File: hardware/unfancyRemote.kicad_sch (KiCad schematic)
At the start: 32 parts, among them J1 Arduino Analog, J2 Arduino Digital, J3 HALL1, J4 HALL2, J5 PPM, J6 Conn_01x02, Q1 AO3401A, Q2 MMBT3904, SW1 SW_Push, U1 E28-2G4M12S

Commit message: Fixed R and Cs footprint
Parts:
- C1, C2, C3, C4, C5, C6, C7: footprint Capacitor_SMD:C_0201_0603Metric -> Capacitor_SMD:C_0603_1608Metric
- R1, R10, R2, R3, R5, R6, R7, R8, R9: footprint Resistor_SMD:R_0201_0603Metric -> Resistor_SMD:R_0603_1608Metric
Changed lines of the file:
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@@
       (effects (font (size 1.27 1.27)) (justify left))
     )
-    (property "Footprint" "Capacitor_SMD:C_0201_0603Metric" (id 2) (at 31.4452 95.25 0)
+    (property "Footprint" "Capacitor_SMD:C_0603_1608Metric" (id 2) (at 31.4452 95.25 0)
       (effects (font (size 1.27 1.27)) hide)
     )
@@
     (property "Reference" "R10" (id 0) (at 219.71 151.13 90))
     (property "Value" "220" (id 1) (at 219.71 153.67 90))
-    (property "Footprint" "Resistor_SMD:R_0201_0603Metric" (id 2) (at 219.71 159.258 90)
+    (property "Footprint" "Resistor_SMD:R_0603_1608Metric" (id 2) (at 219.71 159.258 90)
       (effects (font (size 1.27 1.27)) hide)
     )
@@
     (property "Reference" "R8" (id 0) (at 219.71 130.81 90))
     (property "Value" "220" (id 1) (at 219.71 133.35 90))
-    (property "Footprint" "Resistor_SMD:R_0201_0603Metric" (id 2) (at 219.71 138.938 90)
+    (property "Footprint" "Resistor_SMD:R_0603_1608Metric" (id 2) (at 219.71 138.938 90)
       (effects (font (size 1.27 1.27)) hide)
     )
@@
       (effects (font (size 1.27 1.27)) (justify left))
     )
-    (property "Footprint" "Capacitor_SMD:C_0201_0603Metric" (id 2) (at 44.1452 95.25 0)
+    (property "Footprint" "Capacitor_SMD:C_0603_1608Metric" (id 2) (at 44.1452 95.25 0)
       (effects (font (size 1.27 1.27)) hide)
     )
@@
     (property "Reference" "R7" (id 0) (at 219.71 119.38 90))
     (property "Value" "220" (id 1) (at 219.71 121.92 90))
-    (property "Footprint" "Resistor_SMD:R_0201_0603Metric" (id 2) (at 219.71 127.508 90)
+    (property "Footprint" "Resistor_SMD:R_0603_1608Metric" (id 2) (at 219.71 127.508 90)
       (effects (font (size 1.27 1.27)) hide)
     )
@@
     (property "Reference" "R3" (id 0) (at 115.57 149.86 90))
     (property "Value" "10K" (id 1) (at 115.57 152.4 90))
-    (property "Footprint" "Resistor_SMD:R_0201_0603Metric" (id 2) (at 115.57 157.988 90)
+    (property "Footprint" "Resistor_SMD:R_0603_1608Metric" (id 2) (at 115.57 157.988 90)
       (effects (font (size 1.27 1.27)) hide)
     )
@@
       (effects (font (size 1.27 1.27)) (justify left))
     )
-    (property "Footprint" "Capacitor_SMD:C_0201_0603Metric" (id 2) (at 36.5252 156.21 0)
+    (property "Footprint" "Capacitor_SMD:C_0603_1608Metric" (id 2) (at 36.5252 156.21 0)
       (effects (font (size 1.27 1.27)) hide)
     )
@@
       (effects (font (size 1.27 1.27)) (justify left))
     )
-    (property "Footprint" "Resistor_SMD:R_0201_0603Metric" (id 2) (at 132.842 162.56 90)
+    (property "Footprint" "Resistor_SMD:R_0603_1608Metric" (id 2) (at 132.842 162.56 90)
       (effects (font (size 1.27 1.27)) hide)
     )
@@
       (effects (font (size 1.27 1.27)) (justify left))
     )
-    (property "Footprint" "Capacitor_SMD:C_0201_0603Metric" (id 2) (at 37.7952 124.46 0)
+    (property "Footprint" "Capacitor_SMD:C_0603_1608Metric" (id 2) (at 37.7952 124.46 0)
       (effects (font (size 1.27 1.27)) hide)
     )
@@
     (property "Reference" "R6" (id 0) (at 140.97 149.86 90))
     (property "Value" "220" (id 1) (at 140.97 152.4 90))
-    (property "Footprint" "Resistor_SMD:R_0201_0603Metric" (id 2) (at 140.97 157.988 90)
+    (property "Footprint" "Resistor_SMD:R_0603_1608Metric" (id 2) (at 140.97 157.988 90)
       (effects (font (size 1.27 1.27)) hide)
     )
@@
       (effects (font (size 1.27 1.27)) (justify left))
     )
-    (property "Footprint" "Resistor_SMD:R_0201_0603Metric" (id 2) (at 102.362 134.62 90)
+    (property "Footprint" "Resistor_SMD:R_0603_1608Metric" (id 2) (at 102.362 134.62 90)
       (effects (font (size 1.27 1.27)) hide)
     )
@@
       (effects (font (size 1.27 1.27)) (justify left))
     )
-    (property "Footprint" "Capacitor_SMD:C_0201_0603Metric" (id 2) (at 56.8452 95.25 0)
+    (property "Footprint" "Capacitor_SMD:C_0603_1608Metric" (id 2) (at 56.8452 95.25 0)
       (effects (font (size 1.27 1.27)) hide)
     )
@@
       (effects (font (size 1.27 1.27)) (justify left))
     )
-    (property "Footprint" "Capacitor_SMD:C_0201_0603Metric" (id 2) (at 46.6852 124.46 0)
+    (property "Footprint" "Capacitor_SMD:C_0603_1608Metric" (id 2) (at 46.6852 124.46 0)
       (effects (font (size 1.27 1.27)) hide)
     )
@@
       (effects (font (size 1.27 1.27)) (justify left))
     )
-    (property "Footprint" "Resistor_SMD:R_0201_0603Metric" (id 2) (at 89.662 153.67 90)
+    (property "Footprint" "Resistor_SMD:R_0603_1608Metric" (id 2) (at 89.662 153.67 90)
       (effects (font (size 1.27 1.27)) hide)
     )
@@
     (property "Reference" "R9" (id 0) (at 219.71 142.24 90))
     (property "Value" "220" (id 1) (at 219.71 144.78 90))
-    (property "Footprint" "Resistor_SMD:R_0201_0603Metric" (id 2) (at 219.71 150.368 90)
+    (property "Footprint" "Resistor_SMD:R_0603_1608Metric" (id 2) (at 219.71 150.368 90)
       (effects (font (size 1.27 1.27)) hide)
     )
@@
       (effects (font (size 1.27 1.27)) (justify left))
     )
-    (property "Footprint" "Capacitor_SMD:C_0201_0603Metric" (id 2) (at 46.6852 156.21 0)
+    (property "Footprint" "Capacitor_SMD:C_0603_1608Metric" (id 2) (at 46.6852 156.21 0)
       (effects (font (size 1.27 1.27)) hide)
     )
@@
     )
     (path "/0bb79875-05c7-4b8a-9d2d-5fca0ef83c84"
-      (reference "C1") (unit 1) (value "1uF") (footprint "Capacitor_SMD:C_0201_0603Metric")
+      (reference "C1") (unit 1) (value "1uF") (footprint "Capacitor_SMD:C_0603_1608Metric")
     )
     (path "/2bdd0934-d399-4141-9e05-32af6ebfbe70"
-      (reference "C2") (unit 1) (value "1uF") (footprint "Capacitor_SMD:C_0201_0603Metric")
+      (reference "C2") (unit 1) (value "1uF") (footprint "Capacitor_SMD:C_0603_1608Metric")
     )
     (path "/932ddb45-4ba3-4bf3-a00a-142bac13b3dc"
-      (reference "C3") (unit 1) (value "1uF") (footprint "Capacitor_SMD:C_0201_0603Metric")
+      (reference "C3") (unit 1) (value "1uF") (footprint "Capacitor_SMD:C_0603_1608Metric")
     )
     (path "/98d191c8-54e5-4218-949e-93d6c9f0649c"
-      (reference "C4") (unit 1) (value "1uF") (footprint "Capacitor_SMD:C_0201_0603Metric")
+      (reference "C4") (unit 1) (value "1uF") (footprint "Capacitor_SMD:C_0603_1608Metric")
     )
     (path "/7d0cb9d6-5ec6-497e-ad4a-cb2f17471870"
-      (reference "C5") (unit 1) (value "1uF") (footprint "Capacitor_SMD:C_0201_0603Metric")
+      (reference "C5") (unit 1) (value "1uF") (footprint "Capacitor_SMD:C_0603_1608Metric")
     )
     (path "/fd964b33-4079-42d1-808e-7b045ef787d6"
-      (reference "C6") (unit 1) (value "1uF") (footprint "Capacitor_SMD:C_0201_0603Metric")
+      (reference "C6") (unit 1) (value "1uF") (footprint "Capacitor_SMD:C_0603_1608Metric")
     )
     (path "/5d21f885-012f-4855-94a0-432475643e72"
-      (reference "C7") (unit 1) (value "1uF") (footprint "Capacitor_SMD:C_0201_0603Metric")
+      (reference "C7") (unit 1) (value "1uF") (footprint "Capacitor_SMD:C_0603_1608Metric")
     )
     (path "/cb2b9799-ee7b-4083-a8a4-b36a98ecd37b"
@@
     )
     (path "/992bfab4-6c3b-4d75-b8a7-dddbe50318ad"
-      (reference "R1") (unit 1) (value "220K") (footprint "Resistor_SMD:R_0201_0603Metric")
+      (reference "R1") (unit 1) (value "220K") (footprint "Resistor_SMD:R_0603_1608Metric")
     )
     (path "/8ee26396-cfa7-4786-be63-57d651d4959b"
-      (reference "R2") (unit 1) (value "100K") (footprint "Resistor_SMD:R_0201_0603Metric")
+      (reference "R2") (unit 1) (value "100K") (footprint "Resistor_SMD:R_0603_1608Metric")
     )
     (path "/4ff4deec-58c6-420b-b444-b84fc0a8e9e7"
-      (reference "R3") (unit 1) (value "10K") (footprint "Resistor_SMD:R_0201_0603Metric")
+      (reference "R3") (unit 1) (value "10K") (footprint "Resistor_SMD:R_0603_1608Metric")
     )
     (path "/5d56809f-4d3c-4763-ae66-15a6a309f1f4"
-      (reference "R5") (unit 1) (value "100K") (footprint "Resistor_SMD:R_0201_0603Metric")
+      (reference "R5") (unit 1) (value "100K") (footprint "Resistor_SMD:R_0603_1608Metric")
     )
     (path "/85f48d28-6046-41c5-9513-483c9a53490c"
-      (reference "R6") (unit 1) (value "220") (footprint "Resistor_SMD:R_0201_0603Metric")
+      (reference "R6") (unit 1) (value "220") (footprint "Resistor_SMD:R_0603_1608Metric")
     )
     (path "/438e5a77-b7e2-4d5b-8594-dd7bb5b6ef83"
-      (reference "R7") (unit 1) (value "220") (footprint "Resistor_SMD:R_0201_0603Metric")
+      (reference "R7") (unit 1) (value "220") (footprint "Resistor_SMD:R_0603_1608Metric")
     )
     (path "/256b9b03-3707-4f36-9649-f69e18c94f2c"
-      (reference "R8") (unit 1) (value "220") (footprint "Resistor_SMD:R_0201_0603Metric")
+      (reference "R8") (unit 1) (value "220") (footprint "Resistor_SMD:R_0603_1608Metric")
     )
     (path "/fbe8653a-4262-4873-bcda-2bcce1ea33c6"
-      (reference "R9") (unit 1) (value "220") (footprint "Resistor_SMD:R_0201_0603Metric")
+      (reference "R9") (unit 1) (value "220") (footprint "Resistor_SMD:R_0603_1608Metric")
     )
     (path "/1facb047-7b62-45cf-9c16-479d2cc87771"
-      (reference "R10") (unit 1) (value "220") (footprint "Resistor_SMD:R_0201_0603Metric")
+      (reference "R10") (unit 1) (value "220") (footprint "Resistor_SMD:R_0603_1608Metric")
     )
     (path "/8e875e7b-f435-48fe-904e-cd96af2470b5"

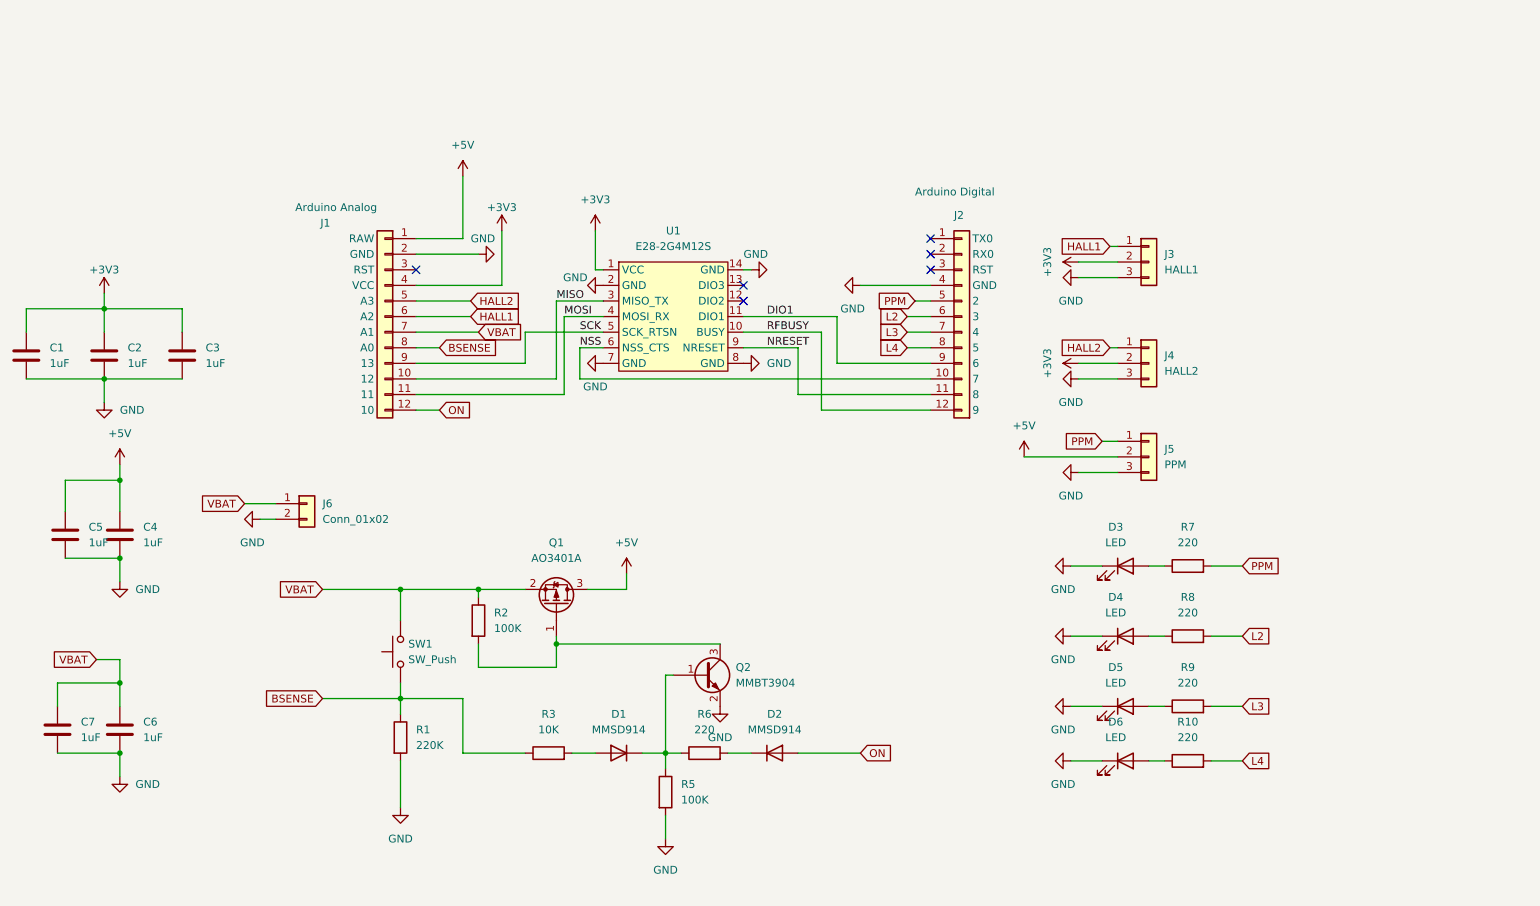
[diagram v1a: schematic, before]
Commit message: Added library, PCB 1.0, software scheduler
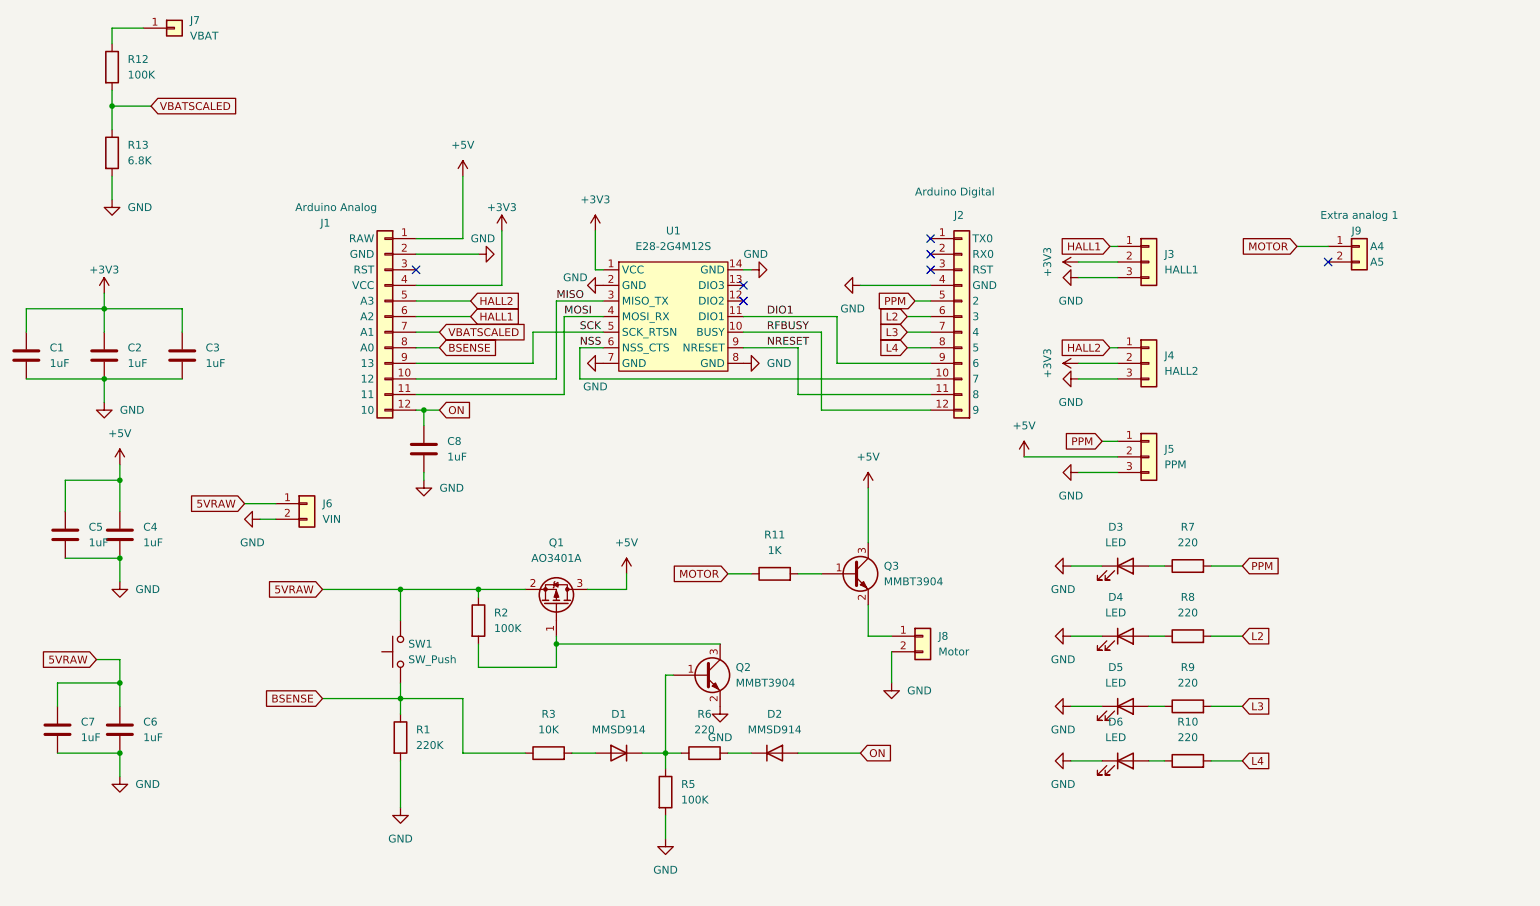
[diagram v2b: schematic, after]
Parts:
- added C8: 1uF, Capacitor_SMD:C_0603_1608Metric, symbol Device:C
- added J7: VBAT, Connector_wire:SolderWirePad_1x01_SMD_1x2mm, symbol Connector_Generic:Conn_01x01
- added J8: Motor, unfancyRemote_components:SolderWirePad_1x02_SMD_1x2mm, symbol Connector_Generic:Conn_01x02
- added J9: Extra analog 1, Connector_PinSocket_2.54mm:PinSocket_1x02_P2.54mm_Vertical, symbol unfancyRemote_components:Extra_analog_1
- added Q3: MMBT3904, Package_TO_SOT_SMD:SOT-23, symbol Transistor_BJT:MMBT3904
- added R11: 1K, Resistor_SMD:R_0603_1608Metric, symbol Device:R
- added R12: 100K, Resistor_SMD:R_0603_1608Metric, symbol Device:R
- added R13: 6.8K, Resistor_SMD:R_0603_1608Metric, symbol Device:R
- J6: value Conn_01x02 -> VIN
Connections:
- net +5V: now also Q3.3 (C)
- net GND: now also C8.2, J8.2 (Pin_2), R13.2
- net ON: now also C8.1
- net VBAT renamed 5VRAW
- net 5VRAW: no longer J1.7 (A1)
- new net: Q3.1 (B), R11.2
- new net: J8.1 (Pin_1), Q3.2 (E)
- new net: J7.1 (Pin_1), R12.1
- new net MOTOR: J9.1 (A4), R11.1
- new net VBATSCALED: J1.7 (A1), R12.2, R13.1
- no-connect marks 6 -> 7
